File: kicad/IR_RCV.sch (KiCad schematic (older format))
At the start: 6 parts, among them U7 AD8604

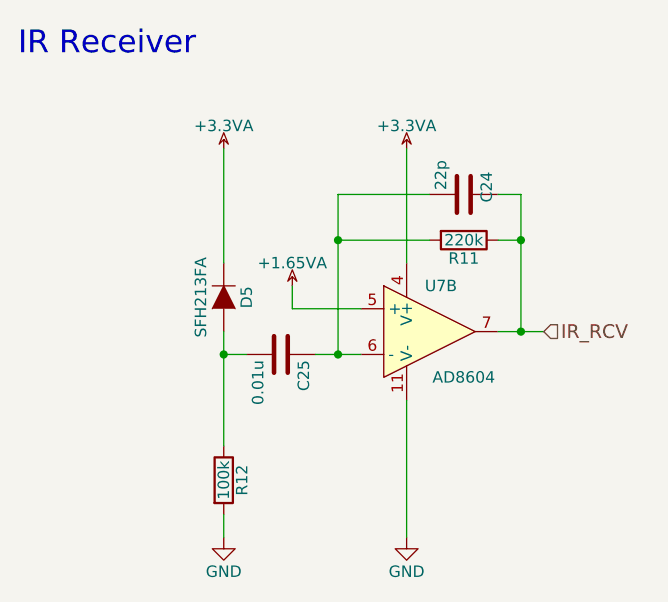
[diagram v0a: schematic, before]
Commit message: フットプリント調整
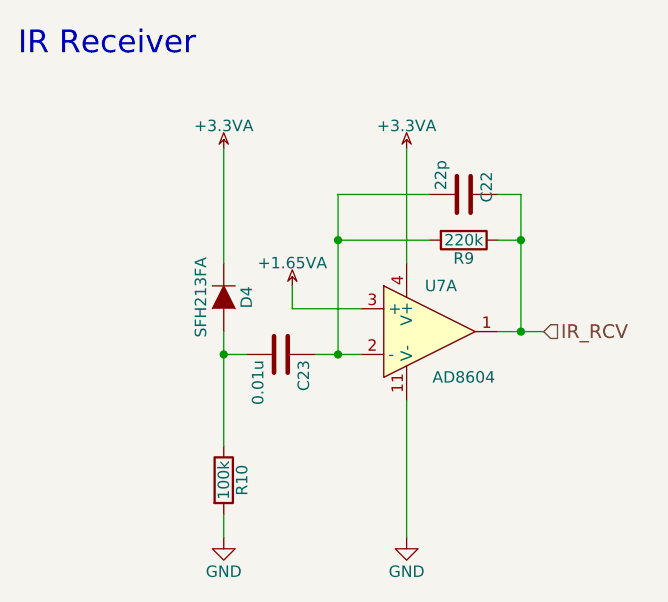
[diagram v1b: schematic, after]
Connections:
- net +1.65VA: now also U7.3 (+); no longer U7.5 (+)
- net IR_RCV: now also U7.1; no longer U7.7
- net at C22.2, C23.1, R9.2: now also U7.2 (-); no longer U7.6 (-)
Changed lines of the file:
@@
 AR Path="/57CF292E/57CF0F37" Ref="D6"  Part="1"
 AR Path="/57CF2A30/57CF0F37" Ref="D7"  Part="1"
-F 0 "D5" H 4600 3950 50  0000 C CNN
+F 0 "D4" H 4600 3950 50  0000 C CNN
 F 1 "SFH213FA" H 4600 3750 50  0000 C CNN
 F 2 "mouse:Photo-5MM_Angle" H 4600 3850 50  0001 C CNN
@@
 $Comp
 L LM2902N U7
-U 2 1 57CF0F3E
+U 1 1 57CF0F3E
 P 5500 4000
 AR Path="/57CF0B09/57CF0F3E" Ref="U7"  Part="1"
@@
 F 2 "Housings_SSOP:TSSOP-14_4.4x5mm_Pitch0.65mm" H 5450 4100 50  0001 C CNN
 F 3 "" H 5550 4200 50  0000 C CNN
-	2    5500 4000
+	1    5500 4000
 	1    0    0    -1
 $EndComp
@@
 AR Path="/57CF292E/57CF0F45" Ref="C27"  Part="1"
 AR Path="/57CF2A30/57CF0F45" Ref="C29"  Part="1"
-F 0 "C25" H 4875 4200 50  0000 L CNN
+F 0 "C23" H 4875 4200 50  0000 L CNN
 F 1 "0.01u" H 4875 4000 50  0000 L CNN
 F 2 "Capacitors_SMD:C_0402" H 4888 3950 50  0001 C CNN
@@
 AR Path="/57CF292E/57CF0F4C" Ref="R14"  Part="1"
 AR Path="/57CF2A30/57CF0F4C" Ref="R16"  Part="1"
-F 0 "R12" V 4680 4650 50  0000 C CNN
+F 0 "R10" V 4680 4650 50  0000 C CNN
 F 1 "100k" V 4600 4650 50  0000 C CNN
 F 2 "Resistors_SMD:R_0402" V 4530 4650 50  0001 C CNN
@@
 AR Path="/57CF292E/57CF0F57" Ref="R13"  Part="1"
 AR Path="/57CF2A30/57CF0F57" Ref="R15"  Part="1"
-F 0 "R11" V 5730 3600 50  0000 C CNN
+F 0 "R9" V 5730 3600 50  0000 C CNN
 F 1 "220k" V 5650 3600 50  0000 C CNN
 F 2 "Resistors_SMD:R_0402" V 5580 3600 50  0001 C CNN
@@
 AR Path="/57CF292E/57CF0F5E" Ref="C26"  Part="1"
 AR Path="/57CF2A30/57CF0F5E" Ref="C28"  Part="1"
-F 0 "C24" H 5550 3500 50  0000 L CNN
+F 0 "C22" H 5550 3500 50  0000 L CNN
 F 1 "22p" H 5500 3300 50  0000 L CNN
 F 2 "Capacitors_SMD:C_0402" H 5688 3250 50  0001 C CNN
@@
 AR Path="/57CF292E/57CF0F71" Ref="#PWR073"  Part="1"
 AR Path="/57CF2A30/57CF0F71" Ref="#PWR078"  Part="1"
-F 0 "#PWR068" H 4750 3150 50  0001 C CNN
+F 0 "#PWR063" H 4750 3150 50  0001 C CNN
 F 1 "+3.3VA" H 4600 3300 50  0000 C CNN
 F 2 "" H 4600 3200 50  0000 C CNN
@@
 AR Path="/57CF292E/57CF0F77" Ref="#PWR074"  Part="1"
 AR Path="/57CF2A30/57CF0F77" Ref="#PWR079"  Part="1"
-F 0 "#PWR069" H 5550 3150 50  0001 C CNN
+F 0 "#PWR064" H 5550 3150 50  0001 C CNN
 F 1 "+3.3VA" H 5400 3300 50  0000 C CNN
 F 2 "" H 5400 3200 50  0000 C CNN
@@
 AR Path="/57CF292E/57CF0F7D" Ref="#PWR075"  Part="1"
 AR Path="/57CF2A30/57CF0F7D" Ref="#PWR080"  Part="1"
-F 0 "#PWR070" H 5050 3750 50  0001 C CNN
+F 0 "#PWR065" H 5050 3750 50  0001 C CNN
 F 1 "+1.65VA" H 4900 3900 50  0000 C CNN
 F 2 "" H 4900 3800 50  0000 C CNN
@@
 AR Path="/57CF292E/57CF0F85" Ref="#PWR076"  Part="1"
 AR Path="/57CF2A30/57CF0F85" Ref="#PWR081"  Part="1"
-F 0 "#PWR071" H 4600 4650 50  0001 C CNN
+F 0 "#PWR066" H 4600 4650 50  0001 C CNN
 F 1 "GND" H 4600 4750 50  0000 C CNN
 F 2 "" H 4600 4900 50  0000 C CNN
@@
 AR Path="/57CF292E/57CF0F8C" Ref="#PWR077"  Part="1"
 AR Path="/57CF2A30/57CF0F8C" Ref="#PWR082"  Part="1"
-F 0 "#PWR072" H 5400 4650 50  0001 C CNN
+F 0 "#PWR067" H 5400 4650 50  0001 C CNN
 F 1 "GND" H 5400 4750 50  0000 C CNN
 F 2 "" H 5400 4900 50  0000 C CNN

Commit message: 徐々に部品を配置，部品の確認
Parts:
- renumbered C22 to C21, C23 to C22, R9 to R8, R10 to R9
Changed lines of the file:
@@
 $Descr A4 11693 8268
 encoding utf-8
-Sheet 7 13
+Sheet 6 13
 Title ""
 Date ""
@@
 $EndComp
 $Comp
-L C C23
+L C C22
 U 1 1 57CF0F45
 P 4850 4100
-AR Path="/57CF0B09/57CF0F45" Ref="C23"  Part="1"
-AR Path="/57CF289D/57CF0F45" Ref="C25"  Part="1"
-AR Path="/57CF292E/57CF0F45" Ref="C27"  Part="1"
-AR Path="/57CF2A30/57CF0F45" Ref="C29"  Part="1"
-F 0 "C23" H 4875 4200 50  0000 L CNN
+AR Path="/57CF0B09/57CF0F45" Ref="C22"  Part="1"
+AR Path="/57CF289D/57CF0F45" Ref="C24"  Part="1"
+AR Path="/57CF292E/57CF0F45" Ref="C26"  Part="1"
+AR Path="/57CF2A30/57CF0F45" Ref="C28"  Part="1"
+F 0 "C22" H 4875 4200 50  0000 L CNN
 F 1 "0.01u" H 4875 4000 50  0000 L CNN
 F 2 "Capacitors_SMD:C_0402" H 4888 3950 50  0001 C CNN
@@
 $EndComp
 $Comp
-L R R10
+L R R9
 U 1 1 57CF0F4C
 P 4600 4650
-AR Path="/57CF0B09/57CF0F4C" Ref="R10"  Part="1"
-AR Path="/57CF289D/57CF0F4C" Ref="R12"  Part="1"
-AR Path="/57CF292E/57CF0F4C" Ref="R14"  Part="1"
-AR Path="/57CF2A30/57CF0F4C" Ref="R16"  Part="1"
-F 0 "R10" V 4680 4650 50  0000 C CNN
+AR Path="/57CF0B09/57CF0F4C" Ref="R9"  Part="1"
+AR Path="/57CF289D/57CF0F4C" Ref="R11"  Part="1"
+AR Path="/57CF292E/57CF0F4C" Ref="R13"  Part="1"
+AR Path="/57CF2A30/57CF0F4C" Ref="R15"  Part="1"
+F 0 "R9" V 4680 4650 50  0000 C CNN
 F 1 "100k" V 4600 4650 50  0000 C CNN
 F 2 "Resistors_SMD:R_0402" V 4530 4650 50  0001 C CNN
@@
 Connection ~ 4600 4100
 $Comp
-L R R9
+L R R8
 U 1 1 57CF0F57
 P 5650 3600
-AR Path="/57CF0B09/57CF0F57" Ref="R9"  Part="1"
-AR Path="/57CF289D/57CF0F57" Ref="R11"  Part="1"
-AR Path="/57CF292E/57CF0F57" Ref="R13"  Part="1"
-AR Path="/57CF2A30/57CF0F57" Ref="R15"  Part="1"
-F 0 "R9" V 5730 3600 50  0000 C CNN
+AR Path="/57CF0B09/57CF0F57" Ref="R8"  Part="1"
+AR Path="/57CF289D/57CF0F57" Ref="R10"  Part="1"
+AR Path="/57CF292E/57CF0F57" Ref="R12"  Part="1"
+AR Path="/57CF2A30/57CF0F57" Ref="R14"  Part="1"
+F 0 "R8" V 5730 3600 50  0000 C CNN
 F 1 "220k" V 5650 3600 50  0000 C CNN
 F 2 "Resistors_SMD:R_0402" V 5580 3600 50  0001 C CNN
@@
 $EndComp
 $Comp
-L C C22
+L C C21
 U 1 1 57CF0F5E
 P 5650 3400
-AR Path="/57CF0B09/57CF0F5E" Ref="C22"  Part="1"
-AR Path="/57CF289D/57CF0F5E" Ref="C24"  Part="1"
-AR Path="/57CF292E/57CF0F5E" Ref="C26"  Part="1"
-AR Path="/57CF2A30/57CF0F5E" Ref="C28"  Part="1"
-F 0 "C22" H 5550 3500 50  0000 L CNN
+AR Path="/57CF0B09/57CF0F5E" Ref="C21"  Part="1"
+AR Path="/57CF289D/57CF0F5E" Ref="C23"  Part="1"
+AR Path="/57CF292E/57CF0F5E" Ref="C25"  Part="1"
+AR Path="/57CF2A30/57CF0F5E" Ref="C27"  Part="1"
+F 0 "C21" H 5550 3500 50  0000 L CNN
 F 1 "22p" H 5500 3300 50  0000 L CNN
 F 2 "Capacitors_SMD:C_0402" H 5688 3250 50  0001 C CNN
@@
 	4600 3200 4600 3700
 $Comp
-L +3.3VA #PWR063
+L +3.3VA #PWR062
 U 1 1 57CF0F71
 P 4600 3200
-AR Path="/57CF0B09/57CF0F71" Ref="#PWR063"  Part="1"
-AR Path="/57CF289D/57CF0F71" Ref="#PWR068"  Part="1"
-AR Path="/57CF292E/57CF0F71" Ref="#PWR073"  Part="1"
-AR Path="/57CF2A30/57CF0F71" Ref="#PWR078"  Part="1"
-F 0 "#PWR063" H 4750 3150 50  0001 C CNN
+AR Path="/57CF0B09/57CF0F71" Ref="#PWR062"  Part="1"
+AR Path="/57CF289D/57CF0F71" Ref="#PWR067"  Part="1"
+AR Path="/57CF292E/57CF0F71" Ref="#PWR072"  Part="1"
+AR Path="/57CF2A30/57CF0F71" Ref="#PWR077"  Part="1"
+F 0 "#PWR062" H 4750 3150 50  0001 C CNN
 F 1 "+3.3VA" H 4600 3300 50  0000 C CNN
 F 2 "" H 4600 3200 50  0000 C CNN
@@
 $EndComp
 $Comp
-L +3.3VA #PWR064
+L +3.3VA #PWR063
 U 1 1 57CF0F77
 P 5400 3200
-AR Path="/57CF0B09/57CF0F77" Ref="#PWR064"  Part="1"
-AR Path="/57CF289D/57CF0F77" Ref="#PWR069"  Part="1"
-AR Path="/57CF292E/57CF0F77" Ref="#PWR074"  Part="1"
-AR Path="/57CF2A30/57CF0F77" Ref="#PWR079"  Part="1"
-F 0 "#PWR064" H 5550 3150 50  0001 C CNN
+AR Path="/57CF0B09/57CF0F77" Ref="#PWR063"  Part="1"
+AR Path="/57CF289D/57CF0F77" Ref="#PWR068"  Part="1"
+AR Path="/57CF292E/57CF0F77" Ref="#PWR073"  Part="1"
+AR Path="/57CF2A30/57CF0F77" Ref="#PWR078"  Part="1"
+F 0 "#PWR063" H 5550 3150 50  0001 C CNN
 F 1 "+3.3VA" H 5400 3300 50  0000 C CNN
 F 2 "" H 5400 3200 50  0000 C CNN
@@
 $EndComp
 $Comp
-L +1.65VA #PWR065
+L +1.65VA #PWR064
 U 1 1 57CF0F7D
 P 4900 3800
-AR Path="/57CF0B09/57CF0F7D" Ref="#PWR065"  Part="1"
-AR Path="/57CF289D/57CF0F7D" Ref="#PWR070"  Part="1"
-AR Path="/57CF292E/57CF0F7D" Ref="#PWR075"  Part="1"
-AR Path="/57CF2A30/57CF0F7D" Ref="#PWR080"  Part="1"
-F 0 "#PWR065" H 5050 3750 50  0001 C CNN
+AR Path="/57CF0B09/57CF0F7D" Ref="#PWR064"  Part="1"
+AR Path="/57CF289D/57CF0F7D" Ref="#PWR069"  Part="1"
+AR Path="/57CF292E/57CF0F7D" Ref="#PWR074"  Part="1"
+AR Path="/57CF2A30/57CF0F7D" Ref="#PWR079"  Part="1"
+F 0 "#PWR064" H 5050 3750 50  0001 C CNN
 F 1 "+1.65VA" H 4900 3900 50  0000 C CNN
 F 2 "" H 4900 3800 50  0000 C CNN
@@
 	4900 3900 5200 3900
 $Comp
-L GND #PWR066
+L GND #PWR065
 U 1 1 57CF0F85
 P 4600 4900
-AR Path="/57CF0B09/57CF0F85" Ref="#PWR066"  Part="1"
-AR Path="/57CF289D/57CF0F85" Ref="#PWR071"  Part="1"
-AR Path="/57CF292E/57CF0F85" Ref="#PWR076"  Part="1"
-AR Path="/57CF2A30/57CF0F85" Ref="#PWR081"  Part="1"
-F 0 "#PWR066" H 4600 4650 50  0001 C CNN
+AR Path="/57CF0B09/57CF0F85" Ref="#PWR065"  Part="1"
+AR Path="/57CF289D/57CF0F85" Ref="#PWR070"  Part="1"
+AR Path="/57CF292E/57CF0F85" Ref="#PWR075"  Part="1"
+AR Path="/57CF2A30/57CF0F85" Ref="#PWR080"  Part="1"
+F 0 "#PWR065" H 4600 4650 50  0001 C CNN
 F 1 "GND" H 4600 4750 50  0000 C CNN
 F 2 "" H 4600 4900 50  0000 C CNN
@@
 	4600 4900 4600 4800
 $Comp
-L GND #PWR067
+L GND #PWR066
 U 1 1 57CF0F8C
 P 5400 4900
-AR Path="/57CF0B09/57CF0F8C" Ref="#PWR067"  Part="1"
-AR Path="/57CF289D/57CF0F8C" Ref="#PWR072"  Part="1"
-AR Path="/57CF292E/57CF0F8C" Ref="#PWR077"  Part="1"
-AR Path="/57CF2A30/57CF0F8C" Ref="#PWR082"  Part="1"
-F 0 "#PWR067" H 5400 4650 50  0001 C CNN
+AR Path="/57CF0B09/57CF0F8C" Ref="#PWR066"  Part="1"
+AR Path="/57CF289D/57CF0F8C" Ref="#PWR071"  Part="1"
+AR Path="/57CF292E/57CF0F8C" Ref="#PWR076"  Part="1"
+AR Path="/57CF2A30/57CF0F8C" Ref="#PWR081"  Part="1"
+F 0 "#PWR066" H 5400 4650 50  0001 C CNN
 F 1 "GND" H 5400 4750 50  0000 C CNN
 F 2 "" H 5400 4900 50  0000 C CNN

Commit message: とりあえず全部品を配置
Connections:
- net +1.65VA: now also U7.10 (+); no longer U7.3 (+)
- net IR_RCV: now also U7.8; no longer U7.1
- net at C21.2, C22.1, R8.2: now also U7.9 (-); no longer U7.2 (-)
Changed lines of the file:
@@
 AR Path="/57CF292E/57CF0F37" Ref="D6"  Part="1"
 AR Path="/57CF2A30/57CF0F37" Ref="D7"  Part="1"
-F 0 "D4" H 4600 3950 50  0000 C CNN
+F 0 "D6" H 4600 3950 50  0000 C CNN
 F 1 "SFH213FA" H 4600 3750 50  0000 C CNN
 F 2 "mouse:Photo-5MM_Angle" H 4600 3850 50  0001 C CNN
@@
 $Comp
 L LM2902N U7
-U 1 1 57CF0F3E
+U 3 1 57CF0F3E
 P 5500 4000
 AR Path="/57CF0B09/57CF0F3E" Ref="U7"  Part="1"
@@
 F 2 "Housings_SSOP:TSSOP-14_4.4x5mm_Pitch0.65mm" H 5450 4100 50  0001 C CNN
 F 3 "" H 5550 4200 50  0000 C CNN
-	1    5500 4000
+	3    5500 4000
 	1    0    0    -1
 $EndComp
@@
 AR Path="/57CF292E/57CF0F45" Ref="C26"  Part="1"
 AR Path="/57CF2A30/57CF0F45" Ref="C28"  Part="1"
-F 0 "C22" H 4875 4200 50  0000 L CNN
+F 0 "C26" H 4875 4200 50  0000 L CNN
 F 1 "0.01u" H 4875 4000 50  0000 L CNN
 F 2 "Capacitors_SMD:C_0402" H 4888 3950 50  0001 C CNN
@@
 AR Path="/57CF292E/57CF0F4C" Ref="R13"  Part="1"
 AR Path="/57CF2A30/57CF0F4C" Ref="R15"  Part="1"
-F 0 "R9" V 4680 4650 50  0000 C CNN
+F 0 "R13" V 4680 4650 50  0000 C CNN
 F 1 "100k" V 4600 4650 50  0000 C CNN
 F 2 "Resistors_SMD:R_0402" V 4530 4650 50  0001 C CNN
@@
 AR Path="/57CF292E/57CF0F57" Ref="R12"  Part="1"
 AR Path="/57CF2A30/57CF0F57" Ref="R14"  Part="1"
-F 0 "R8" V 5730 3600 50  0000 C CNN
+F 0 "R12" V 5730 3600 50  0000 C CNN
 F 1 "220k" V 5650 3600 50  0000 C CNN
 F 2 "Resistors_SMD:R_0402" V 5580 3600 50  0001 C CNN
@@
 AR Path="/57CF292E/57CF0F5E" Ref="C25"  Part="1"
 AR Path="/57CF2A30/57CF0F5E" Ref="C27"  Part="1"
-F 0 "C21" H 5550 3500 50  0000 L CNN
+F 0 "C25" H 5550 3500 50  0000 L CNN
 F 1 "22p" H 5500 3300 50  0000 L CNN
 F 2 "Capacitors_SMD:C_0402" H 5688 3250 50  0001 C CNN
@@
 AR Path="/57CF292E/57CF0F71" Ref="#PWR072"  Part="1"
 AR Path="/57CF2A30/57CF0F71" Ref="#PWR077"  Part="1"
-F 0 "#PWR062" H 4750 3150 50  0001 C CNN
+F 0 "#PWR077" H 4750 3150 50  0001 C CNN
 F 1 "+3.3VA" H 4600 3300 50  0000 C CNN
 F 2 "" H 4600 3200 50  0000 C CNN
@@
 AR Path="/57CF292E/57CF0F77" Ref="#PWR073"  Part="1"
 AR Path="/57CF2A30/57CF0F77" Ref="#PWR078"  Part="1"
-F 0 "#PWR063" H 5550 3150 50  0001 C CNN
+F 0 "#PWR078" H 5550 3150 50  0001 C CNN
 F 1 "+3.3VA" H 5400 3300 50  0000 C CNN
 F 2 "" H 5400 3200 50  0000 C CNN
@@
 AR Path="/57CF292E/57CF0F7D" Ref="#PWR074"  Part="1"
 AR Path="/57CF2A30/57CF0F7D" Ref="#PWR079"  Part="1"
-F 0 "#PWR064" H 5050 3750 50  0001 C CNN
+F 0 "#PWR079" H 5050 3750 50  0001 C CNN
 F 1 "+1.65VA" H 4900 3900 50  0000 C CNN
 F 2 "" H 4900 3800 50  0000 C CNN
@@
 AR Path="/57CF292E/57CF0F85" Ref="#PWR075"  Part="1"
 AR Path="/57CF2A30/57CF0F85" Ref="#PWR080"  Part="1"
-F 0 "#PWR065" H 4600 4650 50  0001 C CNN
+F 0 "#PWR080" H 4600 4650 50  0001 C CNN
 F 1 "GND" H 4600 4750 50  0000 C CNN
 F 2 "" H 4600 4900 50  0000 C CNN
@@
 AR Path="/57CF292E/57CF0F8C" Ref="#PWR076"  Part="1"
 AR Path="/57CF2A30/57CF0F8C" Ref="#PWR081"  Part="1"
-F 0 "#PWR066" H 5400 4650 50  0001 C CNN
+F 0 "#PWR081" H 5400 4650 50  0001 C CNN
 F 1 "GND" H 5400 4750 50  0000 C CNN
 F 2 "" H 5400 4900 50  0000 C CNN

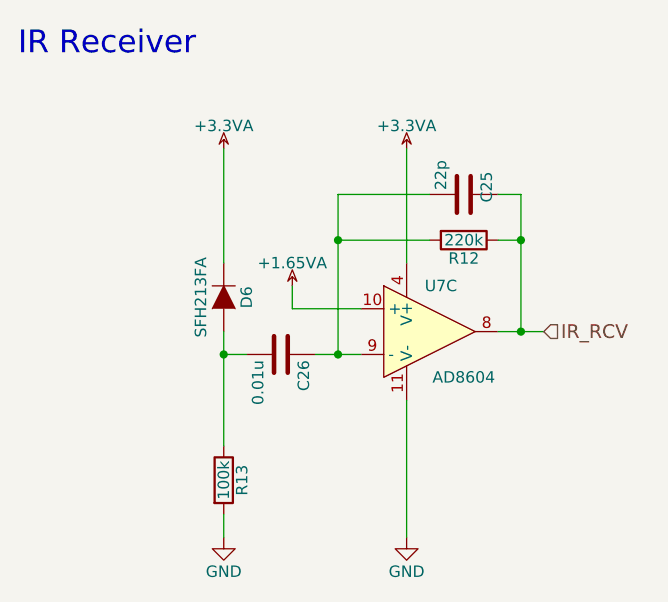
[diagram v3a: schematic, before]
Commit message: ネットリストを更新
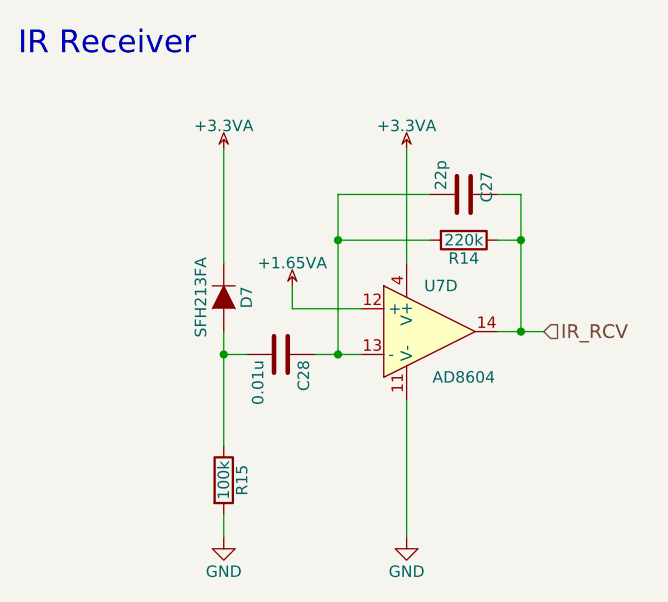
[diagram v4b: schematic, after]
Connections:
- net +1.65VA: now also U7.12 (+); no longer U7.10 (+)
- net IR_RCV: now also U7.14; no longer U7.8
- net at C21.2, C22.1, R8.2: now also U7.13 (-); no longer U7.9 (-)
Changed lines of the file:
@@
 AR Path="/57CF292E/57CF0F37" Ref="D6"  Part="1"
 AR Path="/57CF2A30/57CF0F37" Ref="D7"  Part="1"
-F 0 "D6" H 4600 3950 50  0000 C CNN
+F 0 "D7" H 4600 3950 50  0000 C CNN
 F 1 "SFH213FA" H 4600 3750 50  0000 C CNN
 F 2 "mouse:Photo-5MM_Angle" H 4600 3850 50  0001 C CNN
@@
 $Comp
 L LM2902N U7
-U 3 1 57CF0F3E
+U 4 1 57CF0F3E
 P 5500 4000
 AR Path="/57CF0B09/57CF0F3E" Ref="U7"  Part="1"
@@
 F 2 "Housings_SSOP:TSSOP-14_4.4x5mm_Pitch0.65mm" H 5450 4100 50  0001 C CNN
 F 3 "" H 5550 4200 50  0000 C CNN
-	3    5500 4000
+	4    5500 4000
 	1    0    0    -1
 $EndComp
@@
 AR Path="/57CF292E/57CF0F45" Ref="C26"  Part="1"
 AR Path="/57CF2A30/57CF0F45" Ref="C28"  Part="1"
-F 0 "C26" H 4875 4200 50  0000 L CNN
+F 0 "C28" H 4875 4200 50  0000 L CNN
 F 1 "0.01u" H 4875 4000 50  0000 L CNN
 F 2 "Capacitors_SMD:C_0402" H 4888 3950 50  0001 C CNN
@@
 AR Path="/57CF292E/57CF0F4C" Ref="R13"  Part="1"
 AR Path="/57CF2A30/57CF0F4C" Ref="R15"  Part="1"
-F 0 "R13" V 4680 4650 50  0000 C CNN
+F 0 "R15" V 4680 4650 50  0000 C CNN
 F 1 "100k" V 4600 4650 50  0000 C CNN
 F 2 "Resistors_SMD:R_0402" V 4530 4650 50  0001 C CNN
@@
 AR Path="/57CF292E/57CF0F57" Ref="R12"  Part="1"
 AR Path="/57CF2A30/57CF0F57" Ref="R14"  Part="1"
-F 0 "R12" V 5730 3600 50  0000 C CNN
+F 0 "R14" V 5730 3600 50  0000 C CNN
 F 1 "220k" V 5650 3600 50  0000 C CNN
 F 2 "Resistors_SMD:R_0402" V 5580 3600 50  0001 C CNN
@@
 AR Path="/57CF292E/57CF0F5E" Ref="C25"  Part="1"
 AR Path="/57CF2A30/57CF0F5E" Ref="C27"  Part="1"
-F 0 "C25" H 5550 3500 50  0000 L CNN
+F 0 "C27" H 5550 3500 50  0000 L CNN
 F 1 "22p" H 5500 3300 50  0000 L CNN
 F 2 "Capacitors_SMD:C_0402" H 5688 3250 50  0001 C CNN

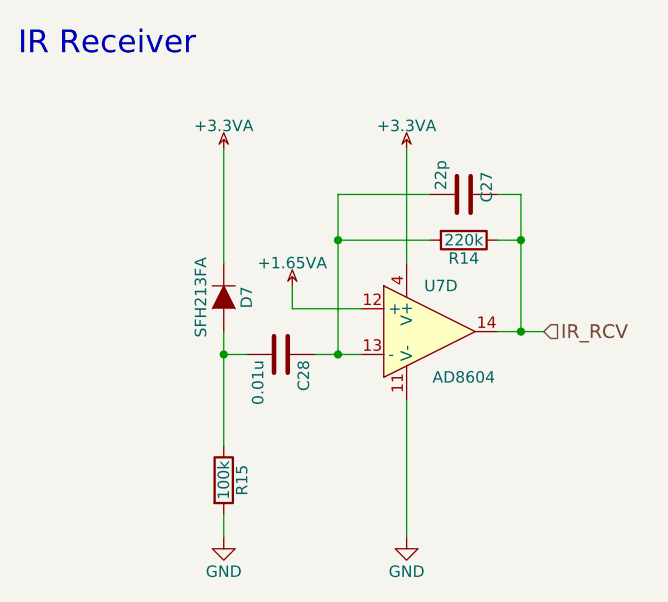
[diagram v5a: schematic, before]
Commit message: 充電基板を階層に．
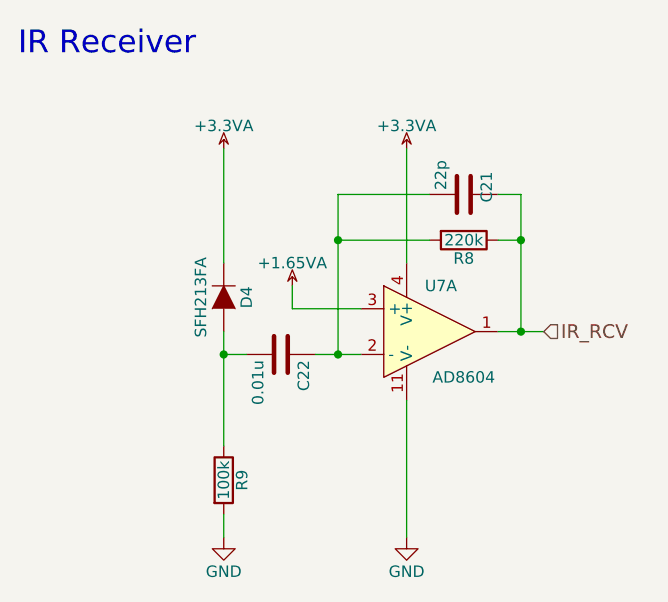
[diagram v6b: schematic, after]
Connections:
- net +1.65VA: now also U7.3 (+); no longer U7.12 (+)
- net IR_RCV: now also U7.1; no longer U7.14
- net at C21.2, C22.1, R8.2: now also U7.2 (-); no longer U7.13 (-)
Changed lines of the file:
@@
 $Descr A4 11693 8268
 encoding utf-8
-Sheet 6 14
+Sheet 6 15
 Title ""
 Date ""
@@
 AR Path="/57CF292E/57CF0F37" Ref="D6"  Part="1"
 AR Path="/57CF2A30/57CF0F37" Ref="D7"  Part="1"
-F 0 "D7" H 4600 3950 50  0000 C CNN
+F 0 "D4" H 4600 3950 50  0000 C CNN
 F 1 "SFH213FA" H 4600 3750 50  0000 C CNN
 F 2 "mouse:Photo-5MM_Angle" H 4600 3850 50  0001 C CNN
@@
 $Comp
 L LM2902N U7
-U 4 1 57CF0F3E
+U 1 1 57CF0F3E
 P 5500 4000
 AR Path="/57CF0B09/57CF0F3E" Ref="U7"  Part="1"
@@
 F 2 "Housings_SSOP:TSSOP-14_4.4x5mm_Pitch0.65mm" H 5450 4100 50  0001 C CNN
 F 3 "" H 5550 4200 50  0000 C CNN
-	4    5500 4000
+	1    5500 4000
 	1    0    0    -1
 $EndComp
@@
 AR Path="/57CF292E/57CF0F45" Ref="C26"  Part="1"
 AR Path="/57CF2A30/57CF0F45" Ref="C28"  Part="1"
-F 0 "C28" H 4875 4200 50  0000 L CNN
+F 0 "C22" H 4875 4200 50  0000 L CNN
 F 1 "0.01u" H 4875 4000 50  0000 L CNN
 F 2 "Capacitors_SMD:C_0402" H 4888 3950 50  0001 C CNN
@@
 AR Path="/57CF292E/57CF0F4C" Ref="R13"  Part="1"
 AR Path="/57CF2A30/57CF0F4C" Ref="R15"  Part="1"
-F 0 "R15" V 4680 4650 50  0000 C CNN
+F 0 "R9" V 4680 4650 50  0000 C CNN
 F 1 "100k" V 4600 4650 50  0000 C CNN
 F 2 "Resistors_SMD:R_0402" V 4530 4650 50  0001 C CNN
@@
 AR Path="/57CF292E/57CF0F57" Ref="R12"  Part="1"
 AR Path="/57CF2A30/57CF0F57" Ref="R14"  Part="1"
-F 0 "R14" V 5730 3600 50  0000 C CNN
+F 0 "R8" V 5730 3600 50  0000 C CNN
 F 1 "220k" V 5650 3600 50  0000 C CNN
 F 2 "Resistors_SMD:R_0402" V 5580 3600 50  0001 C CNN
@@
 AR Path="/57CF292E/57CF0F5E" Ref="C25"  Part="1"
 AR Path="/57CF2A30/57CF0F5E" Ref="C27"  Part="1"
-F 0 "C27" H 5550 3500 50  0000 L CNN
+F 0 "C21" H 5550 3500 50  0000 L CNN
 F 1 "22p" H 5500 3300 50  0000 L CNN
 F 2 "Capacitors_SMD:C_0402" H 5688 3250 50  0001 C CNN
